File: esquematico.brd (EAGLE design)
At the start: 200 x 139.8 mm, 18 parts

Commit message: Design Board.
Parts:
- removed U$2: DRV8833, DRV8833:DRV8833
- added U1: ROB-14450, ROB-14450:MODULE_ROB-14450
- moved R5 185.1 mm to (-177.8, 115.6)
- moved LED2 180.7 mm to (-163.8, 109.2)
- moved R4 177.1 mm to (-170.2, 115.6)
- moved R3 169.2 mm to (-162.6, 115.6)
- moved U$3 167.4 mm to (-163.8, 68.6)
- moved LED1 166.9 mm to (-151.1, 109.2)
- moved R2 161.3 mm to (-154.9, 115.6)
- moved R1 153.5 mm to (-147.3, 115.6)
- moved S1 149.1 mm to (-149.9, 94.0)
- moved S2 149.1 mm to (-160.0, 94.0)
- moved X2 148.4 mm to (-127.0, 96.5)
- moved X3 148.4 mm to (-138.4, 96.5)
- moved DISPLAY 114.3 mm to (-11.4, 104.1)
- moved MUX 99.4 mm to (2.54, 132.1), flipped to the top
- moved S3 98.2 mm to (-40.6, 104.1)
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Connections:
- removed net AIN1: U$1.P$6, U$2.11
- removed net AIN2: U$1.P$5, U$2.10
- removed net BIN1: U$1.P$10, U$2.13
- removed net BIN2: U$1.P$11, U$2.14
- new net AI1: U$1.P$7, U1.14
- new net AI2: U$1.P$6, U1.15
- new net BI1: U$1.P$9, U1.12
- new net BI2: U$1.P$10, U1.11
- new net PWMA: U$1.P$5, U1.16
- new net PWMB: U$1.P$11, U1.10
- net A01: now also U1.4; no longer U$2.4
- net A02: now also U1.5; no longer U$2.5
- net B01: now also U1.7; no longer U$2.7
- net B02: now also U1.6; no longer U$2.6
- net GND: now also U1.3, U1.8, U1.9; no longer U$2.16, U$2.3, U$2.8
- net STBY: now also U1.13; no longer U$2.12
- net VCC: now also U1.1, U1.2; no longer U$2.1
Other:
- board size 200 x 139.8 mm -> 180.8 x 139.8 mm

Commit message: Att Lib
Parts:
- removed DISPLAY: (no value), pinhead:1X08
- added U$2: NOKIA5110, DRV8833:1X08
- moved R5 205.0 mm to (26.7, 130.8)
- moved R4 197.9 mm to (26.7, 135.9), flipped to the bottom
- moved X2 183.6 mm to (45.7, 34.3), turned to 90 degrees
- moved U$3 137.0 mm to (-29.2, 43.2), turned to 90 degrees
- moved LED2 135.1 mm to (-30.5, 130.8)
- moved LED1 133.8 mm to (-19.1, 130.8)
- moved R3 131.1 mm to (-33.0, 95.2), turned to 270 degrees
- moved S2 120.9 mm to (-40.6, 113.0)
- moved R2 117.3 mm to (-39.4, 95.2), turned to 90 degrees
- moved X3 113.8 mm to (-43.2, 34.3), turned to 270 degrees
- moved S1 112.7 mm to (-40.6, 121.9)
- moved R1 101.1 mm to (-48.3, 95.2), turned to 270 degrees
- moved U1 36.9 mm to (35.6, 101.6)
- moved X1 12.0 mm to (44.5, 48.3)
- moved U$1 10.9 mm to (-5.08, 61.0)
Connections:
- net BL: now also U$2.7; no longer DISPLAY.7
- net CE: now also U$2.2; no longer DISPLAY.2
- net CLK: now also U$2.5; no longer DISPLAY.5
- net DC: now also U$2.3; no longer DISPLAY.3
- net DIN: now also U$2.4; no longer DISPLAY.4
- net GND: now also U$2.8; no longer DISPLAY.8
- net RST: now also U$2.1; no longer DISPLAY.1
- net VCC: now also U$1.P$23, U$2.6; no longer DISPLAY.6
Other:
- outline, holes or cut-outs redrawn

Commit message: Trilhas V1
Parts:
- removed LED1, LED2: (no value), led:LED5MM
- removed R3, R4, R5: (no value), rcl:0204/5
- removed S3: (no value), switch-omron:B3F-10XX
- R1, R2: device rcl:0204/5 -> rcl:0204/7
- moved S1 111.9 mm to (45.7, 50.8), turned to 90 degrees
- moved X3 104.2 mm to (61.0, 30.5)
- moved S2 100.2 mm to (45.7, 62.2), turned to 90 degrees
- moved X2 94.1 mm to (-48.3, 29.2), turned to 270 degrees
- moved X1 92.8 mm to (-48.3, 44.5), turned to 90 degrees
- moved R1 49.9 mm to (-35.6, 47.0), turned to 180 degrees
- moved R2 44.6 mm to (-35.6, 50.8), turned to 180 degrees
- moved U$3 31.8 mm to (-27.9, 74.9), turned to 180 degrees
- moved U1 11.4 mm to (35.6, 90.2)
- moved U$2 10.2 mm to (-8.89, 116.8)
- moved U$1 3.59 mm to (-7.62, 63.5)
- moved MUX 1.27 mm to (1.27, 132.1), turned to 180 degrees
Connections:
- removed net BOT3: R3.1, S3.1, S3.2, U$1.P$16
- removed net EN_LED1: R4.1, U$1.P$12
- removed net EN_LED2: R5.1, U$1.P$13
- removed net N$1: LED1.A, R4.2
- removed net N$2: LED2.A, R5.2
- net BOT1: now also U$1.P$17; no longer U$1.P$14
- net BOT2: now also U$1.P$16; no longer U$1.P$15
- net GND: no longer LED1.K, LED2.K, S3.3, S3.4
- net VCC: no longer R3.2
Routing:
- net GND: track 0.00 -> 450.7 mm
- net VCC: track 0.00 -> 373.4 mm
- net A02: track 0.00 -> 188.3 mm
- net A01: track 0.00 -> 178.9 mm
- net BOT1: track 0.00 -> 118.4 mm
- net BOT2: track 0.00 -> 85.8 mm
- net B02: track 0.00 -> 85.5 mm
- net B01: track 0.00 -> 82.5 mm
- net PWMB: track 0.00 -> 79.7 mm
- net BI2: track 0.00 -> 77.1 mm
- net BI1: track 0.00 -> 74.6 mm
- net STBY: track 0.00 -> 71.3 mm
- net AI1: track 0.00 -> 68.0 mm
- net S0: track 0.00 -> 67.3 mm
- net EN: track 0.00 -> 67.3 mm
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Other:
- outline, holes or cut-outs redrawn

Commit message: Trilhas V2
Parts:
- moved MUX 1.27 mm to (1.27, 130.8)
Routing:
- net B01: track 82.5 -> 93.7 mm
- net GND: track 450.7 -> 455.7 mm
- net SIG: track 66.2 -> 65.0 mm
- net S3: track 66.2 -> 65.0 mm
- net S2: track 66.2 -> 65.0 mm
- net S1: track 66.2 -> 65.0 mm
- net S0: track 67.3 -> 66.0 mm
- net EN: track 67.3 -> 66.0 mm
- net VCC: track 373.4 -> 372.9 mm

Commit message: Trilhas V3
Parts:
- moved U$3 14.7 mm to (-28.9, 60.2), turned to 90 degrees
- moved U$2 6.35 mm to (-2.54, 116.8)
- moved MUX 2.84 mm to (-1.27, 129.5), turned to 0 degrees
- moved R1 2.00 mm to (-35.6, 45.0)
- moved X3 1.60 mm to (62.6, 30.5)
- moved R2 1.00 mm to (-35.6, 49.8)
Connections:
- removed net +5V: U$1.P$21
- net VCC: now also U$1.P$21; no longer U$1.P$23
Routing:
- net GND: track 455.7 -> 357.1 mm
- net EN: track 66.0 -> 94.6 mm
- net S0: track 66.0 -> 89.5 mm
- net S1: track 65.0 -> 85.5 mm
- net VCC: track 372.9 -> 391.3 mm
- net S2: track 65.0 -> 81.7 mm
- net A01: track 178.9 -> 162.7 mm
- net +7.4V: track 60.3 -> 44.3 mm
- net A02: track 188.3 -> 173.7 mm
- net B01: track 93.7 -> 84.0 mm
- net S3: track 65.0 -> 74.6 mm
- net PWMA: track 59.3 -> 63.8 mm
- net SIG: track 65.0 -> 60.5 mm
- net CLK: track 16.5 -> 12.4 mm
- net AI2: track 63.7 -> 67.4 mm
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- added copper zone on layer 16, net GND

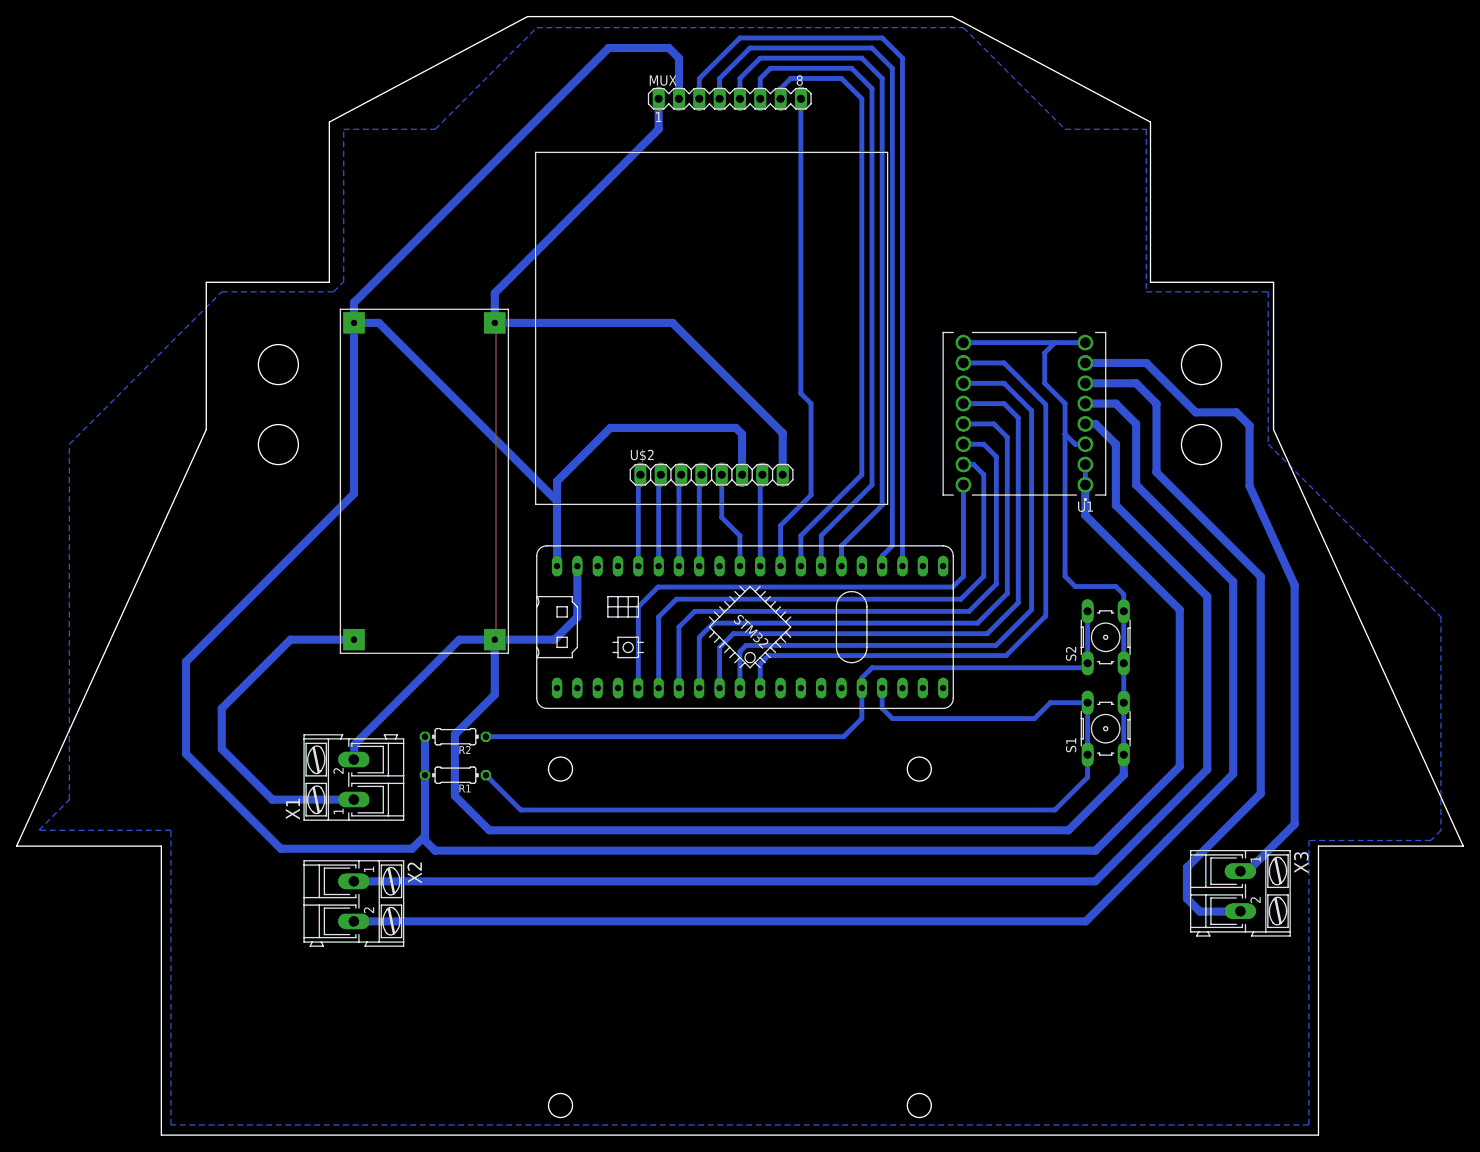
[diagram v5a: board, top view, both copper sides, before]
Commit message: Atualização furos PCB/Trilhas
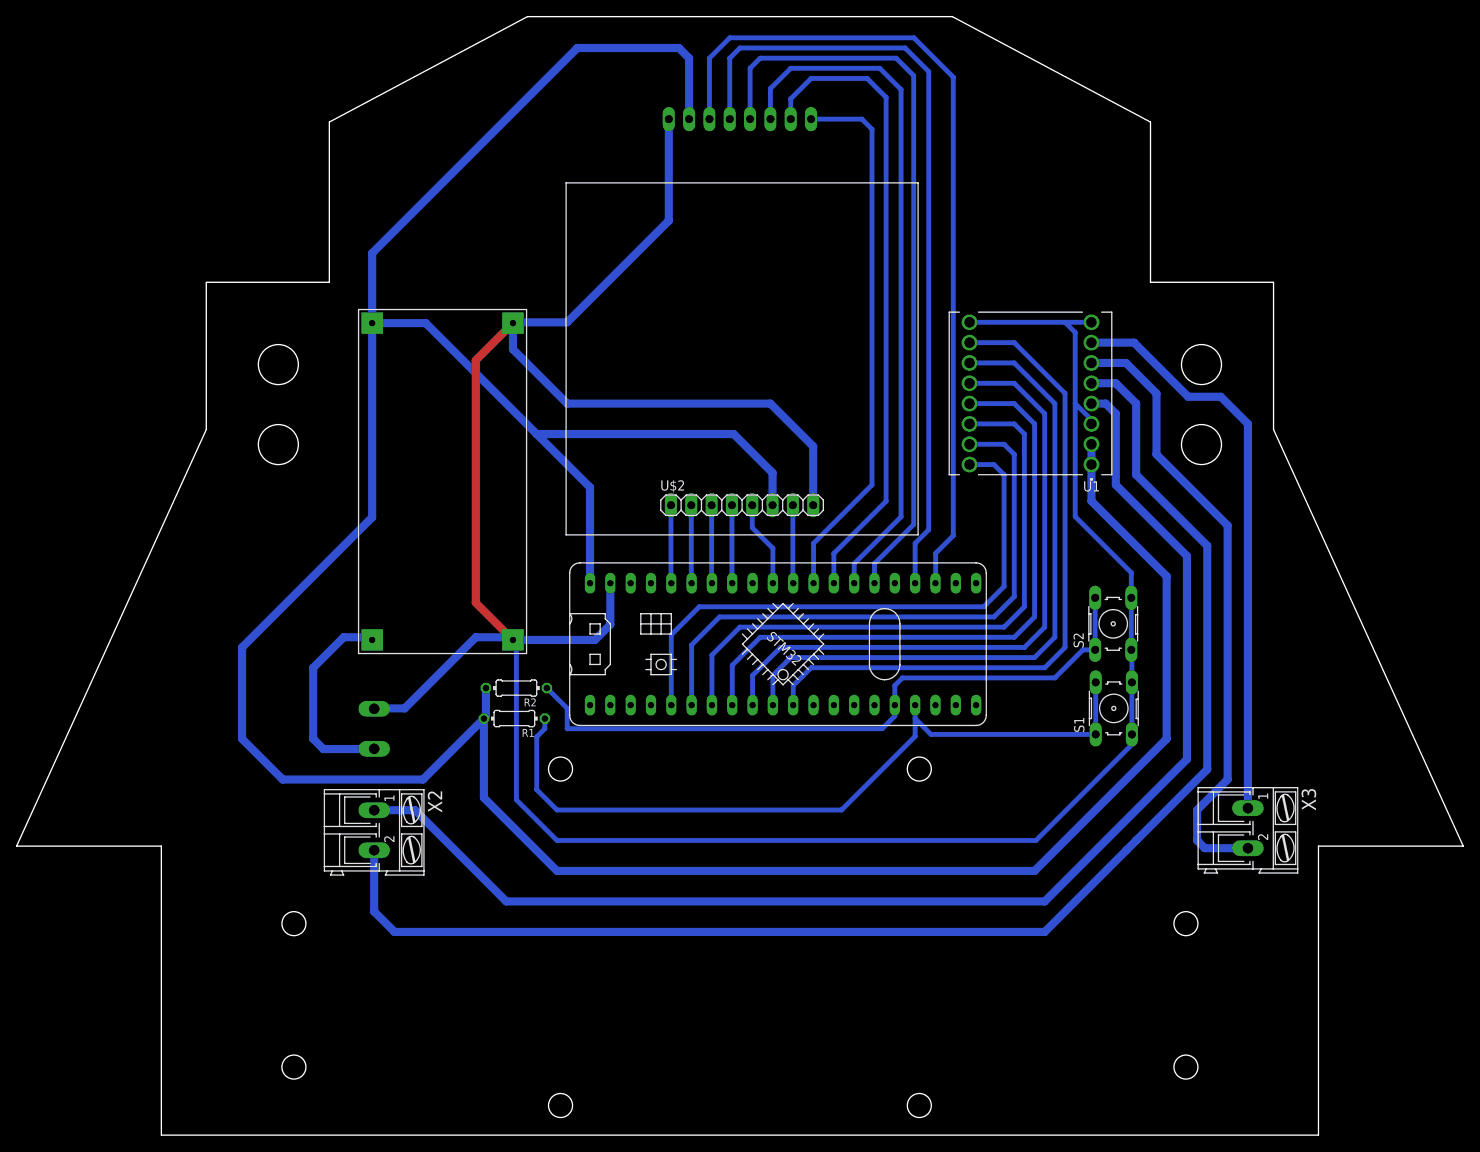
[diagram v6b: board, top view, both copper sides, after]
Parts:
- moved R1 10.2 mm to (-28.2, 52.1)
- moved R2 9.75 mm to (-27.9, 55.9)
- moved X2 9.25 mm to (-45.7, 38.1)
- moved X3 7.93 mm to (63.5, 38.4)
- moved X1 6.84 mm to (-45.7, 50.8), flipped to the bottom
- moved U$2 5.39 mm to (1.27, 113.0)
- moved U$1 4.64 mm to (-3.50, 61.4)
- moved MUX 2.84 mm to (0.00, 127.0), flipped to the bottom, turned to 180 degrees
- moved S1 2.74 mm to (46.7, 53.3)
- moved U1 2.65 mm to (36.3, 92.7)
- moved U$3 2.27 mm to (-26.7, 60.2)
- moved S2 1.93 mm to (46.7, 63.9)
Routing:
- net BOT1: track 117.6 -> 95.3 mm
- net +7.4V: track 44.3 -> 26.1 mm
- net B01: track 84.0 -> 71.8 mm
- net B02: track 88.4 -> 77.6 mm
- net EN: track 94.6 -> 105.4 mm
- net S0: track 89.5 -> 98.9 mm
- net S1: track 85.5 -> 93.7 mm
- net PWMA: track 63.8 -> 71.7 mm
- net SIG: track 60.5 -> 67.9 mm
- net AI2: track 67.4 -> 74.2 mm
- net AI1: track 70.2 -> 76.8 mm
- net STBY: track 72.8 -> 78.6 mm
- net S3: track 74.6 -> 79.9 mm
- net BI1: track 75.4 -> 80.4 mm
- net BI2: track 78.0 -> 82.9 mm
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- removed copper zone on layer 16, net GND

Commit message: Trilhas V4
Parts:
- removed MUX: (no value), con-lstb:MA08-1
- added SV1: (no value), con-amp-mt:S08P
- moved X3 10.9 mm to (67.3, 48.5)
- moved S2 2.37 mm to (45.3, 65.8)
- moved S1 1.52 mm to (45.4, 52.7)
- flipped X1 to the top
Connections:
- net EN: now also SV1.6; no longer MUX.3
- net GND: now also SV1.8; no longer MUX.1
- net S0: now also SV1.5; no longer MUX.4
- net S1: now also SV1.4; no longer MUX.5
- net S2: now also SV1.3; no longer MUX.6
- net S3: now also SV1.2; no longer MUX.7
- net SIG: now also SV1.1; no longer MUX.8
- net VCC: now also SV1.7; no longer MUX.2
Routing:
- net B02: track 77.6 -> 64.4 mm
- net B01: track 71.8 -> 63.2 mm
- net VCC: track 395.5 -> 391.6 mm
- net PWMA: track 71.7 -> 68.6 mm
- net AI1: track 76.8 -> 73.8 mm
- net AI2: track 74.2 -> 71.5 mm
- net STBY: track 78.6 -> 76.2 mm
- net BI2: track 82.9 -> 80.7 mm
- net BI1: track 80.4 -> 78.2 mm
- net BOT1: track 95.3 -> 93.2 mm
- net PWMB: track 84.7 -> 82.8 mm
- net A01: track 164.1 -> 165.2 mm
- net EN: track 105.4 -> 104.3 mm
- net BOT2: track 84.9 -> 85.8 mm
- net GND: track 352.5 -> 353.2 mm, vias 0 -> 1
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- added copper zone on layer 16, net GND

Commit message: Trilhas V5
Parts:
- moved U1 1.27 mm to (35.1, 92.7)
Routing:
- net S1: track 93.7 -> 85.4 mm
- net S3: track 80.0 -> 72.3 mm
- net S2: track 86.5 -> 79.0 mm
- net S0: track 98.9 -> 91.5 mm
- net EN: track 104.3 -> 97.8 mm
- net SIG: track 67.6 -> 61.6 mm
- net AI2: track 71.5 -> 74.4 mm
- net B02: track 64.4 -> 65.6 mm
- net A02: track 177.3 -> 178.6 mm
- net B01: track 63.2 -> 64.5 mm
- net GND: track 353.2 -> 354.3 mm
- net STBY: track 76.2 -> 77.2 mm
- net BI2: track 80.7 -> 81.6 mm
- net BI1: track 78.2 -> 79.1 mm
- net AI1: track 73.8 -> 74.7 mm
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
